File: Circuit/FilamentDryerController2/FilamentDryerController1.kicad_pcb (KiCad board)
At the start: 2 copper layers, 37 parts, among them J1 PWR, J2 Fan, J3 I2C, J4 Heat, J5 I2C, J6 100k, Q1 IRL540N or IRFZ20 or IRF740 o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, SW1 Push, U1 ATmega328-P, U2 LM7805_TO220, U3 SN74LVC2G06, Y1 16MHz

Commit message: Pcb done.
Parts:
- removed C2: 100nF, SparkFun-Capacitor:C_1206_3216Metric
- removed the C4 at (162.5, 46.5)
- removed the J1 at (56.0, 49.0)
- removed the J4 at (69.5, 37.0)
- removed NT1: NetTie, NetTie:NetTie-2_SMD_Pad2.0mm
- removed NT2: NetTie, NetTie:NetTie-2_SMD_Pad0.5mm
- added J5: Screw_Terminal_01x04, SparkFun-Connector:Screw_Terminal_3.5mm-4, F.Cu at (22.5, 26.5)
- added NT4: Mains, Halojen-Footprints:NetTie-2_SMD_Pad0.2x2.5mm, F.Cu at (30.0, 48.0)
- added PS1: HLK-PM01, Converter_ACDC:Converter_ACDC_Hi-Link_HLK-PMxx, F.Cu at (34.0, 33.5)
- added Q2: T835-600B, Package_TO_SOT_SMD:TO-252-2, F.Cu at (36.4, 53.3)
- added R3: 330R, Resistor_SMD:R_1206_3216Metric, F.Cu at (60.2, 57.1)
- added R4: 330R, Resistor_SMD:R_1206_3216Metric, F.Cu at (26.7, 52.6)
- added R5: 360R, Resistor_SMD:R_1206_3216Metric, F.Cu at (46.7, 50.0)
- added TP10: PD3, SparkFun-Connector:TestPoint-1.25mm, F.Cu at (43.6, 79.2)
- added TP7: PC6, SparkFun-Connector:TestPoint-1.25mm, F.Cu at (43.6, 69.1)
- C1, C3: footprint SparkFun-Capacitor:C_1206_3216Metric -> Capacitor_SMD:C_1206_3216Metric
- C4: renamed from C5; footprint SparkFun-Capacitor:C_1206_3216Metric -> Capacitor_SMD:C_1206_3216Metric
- C5: renamed from C6; footprint SparkFun-Capacitor:C_1206_3216Metric -> Capacitor_SMD:C_1206_3216Metric
- J3: renamed from J2; footprint Connector_JST:JST_XH_B4B-XH-A_1x04_P2.50mm_Vertical -> Connector_JST:JST_XH_B2B-XH-A_1x02_P2.50mm_Vertical
- J4: renamed from J6; footprint Connector_JST:JST_XH_B2B-XH-AM_1x02_P2.50mm_Vertical -> Connector_JST:JST_XH_B2B-XH-A_1x02_P2.50mm_Vertical
- NT3: value NetTie -> Mains; footprint NetTie:NetTie-2_SMD_Pad0.5mm -> Halojen-Footprints:NetTie-2_SMD_Pad0.2x2.5mm
- Q1: value IRL540N or IRFZ20 or IRF740 or FDS6690A -> FDS6690A; footprint digikey-footprints:TO-220-3 -> Package_SO:SOIC-8_3.9x4.9mm_P1.27mm
- R1: value 10k -> 100k
- SW1: footprint SparkFun-Switch:Push_SMD_6.2x6.2mm -> Button_Switch_SMD:SW_SPST_PTS645
- TP1: renamed from TP11; value PB2 -> PB0; footprint SparkFun-Connector:1x01 -> SparkFun-Connector:TestPoint-1.25mm
- TP11: renamed from TP8; footprint SparkFun-Connector:1x01 -> SparkFun-Connector:TestPoint-1.25mm
- TP12: renamed from TP9; footprint SparkFun-Connector:1x01 -> SparkFun-Connector:TestPoint-1.25mm
- TP13: renamed from TP10; footprint SparkFun-Connector:1x01 -> SparkFun-Connector:TestPoint-1.25mm
- TP2: renamed from TP1; footprint SparkFun-Connector:1x01 -> SparkFun-Connector:TestPoint-1.25mm
- TP3: renamed from TP2; footprint SparkFun-Connector:1x01 -> SparkFun-Connector:TestPoint-1.25mm
- TP4: renamed from TP3; footprint SparkFun-Connector:1x01 -> SparkFun-Connector:TestPoint-1.25mm
- TP5: renamed from TP4; footprint SparkFun-Connector:1x01 -> SparkFun-Connector:TestPoint-1.25mm
- TP6: renamed from TP5; footprint SparkFun-Connector:1x01 -> SparkFun-Connector:TestPoint-1.25mm
- TP8: renamed from TP6; footprint SparkFun-Connector:1x01 -> SparkFun-Connector:TestPoint-1.25mm
- TP9: renamed from TP7; footprint SparkFun-Connector:1x01 -> SparkFun-Connector:TestPoint-1.25mm
- U2: value LM7805_TO220 -> MOC3043M; footprint Package_TO_SOT_THT:TO-220-3_Vertical -> Package_DIP:SMDIP-6_W9.53mm
- moved C3 127.4 mm to (42.0, 83.1), turned to 180 degrees
- moved NT3 124.2 mm to (40.6, 48.0), turned to 180 degrees
- moved C1 115.0 mm to (59.7, 86.7), turned to 90 degrees
- moved TP11 89.9 mm to (40.6, 79.2)
- moved TP9 87.7 mm to (43.6, 74.2)
- moved TP8 87.3 mm to (43.6, 71.6)
- moved TP12 86.9 mm to (40.6, 99.6)
- moved TP1 84.1 mm to (43.7, 102.1)
- moved TP13 84.1 mm to (43.6, 99.6)
- moved J3 82.8 mm to (22.6, 70.1), turned to 90 degrees
- moved TP5 70.8 mm to (59.6, 76.7)
- moved TP6 70.2 mm to (59.6, 74.2)
- moved TP4 67.8 mm to (59.6, 79.2)
- moved TP3 61.4 mm to (59.6, 97.0)
- moved TP2 60.8 mm to (59.6, 99.6)
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- renumbered J3 to J1, J5 to J2, R3 to R6
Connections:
- C4 pad 2: GNDS -> GND
- C5 pad 1: GNDS -> GND
- J3 pad 1: GND -> +5V
- J3 pad 2: +12V -> Net-(J3-Pin_2)
- J4 pad 1: +5VS -> +5V
- NT3 pad 1: GND -> Net-(NT3-Pad1)
- NT3 pad 2: GNDS -> +AC
- Q1 pad 1: /pHeat -> GND
- Q1 pad 2: Net-(J4-Pin_2) -> GND
- Q1 pad 3: GND12V -> GND
- R1 pad 1: /pHeat -> /pFan_pwm
- R1 pad 2: GNDS -> GND
- R2 pad 2: GNDS -> GND
- SW1 pad 1: GNDS -> GND
- U2 pad 1: +12V -> +5V
- U2 pad 2: GND -> Net-(R3-Pad2)
- U2 pad 3: +5V -> unconnected-(U2-NC-Pad3)
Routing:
- net +5V: track 0.00 -> 182.5 mm, vias 0 -> 4
- net /pHeat: track 0.00 -> 53.5 mm
- net GND: track 0.00 -> 48.1 mm, vias 0 -> 3
- net /pFan_pwm: track 0.00 -> 47.7 mm
- net +AC: track 0.00 -> 36.7 mm
- net /pSCL: track 0.00 -> 34.8 mm
- net /pSDA: track 0.00 -> 32.7 mm, vias 0 -> 1
- net Net-(Q2-G): track 0.00 -> 24.3 mm
- net /pButt: track 0.00 -> 18.3 mm
- net /pTemp: track 0.00 -> 18.2 mm
- net Heater: track 0.00 -> 17.7 mm
- net -AC: track 0.00 -> 17.1 mm
- net Net-(R5-Pad1): track 0.00 -> 13.4 mm, vias 0 -> 2
- net Net-(J3-Pin_2): track 0.00 -> 11.0 mm
- net Net-(U1-PD6): track 0.00 -> 8.16 mm
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- added copper zone on F.Cu, net (none)
- added copper zone on B.Cu, net GND
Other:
- board outline added: 54.1 x 82.3 mm
- board text added: "Filament dryer v0.1 2025 Halojen Productions"
- board text added: "H"
- board text added: "L"
- board text added: "N"

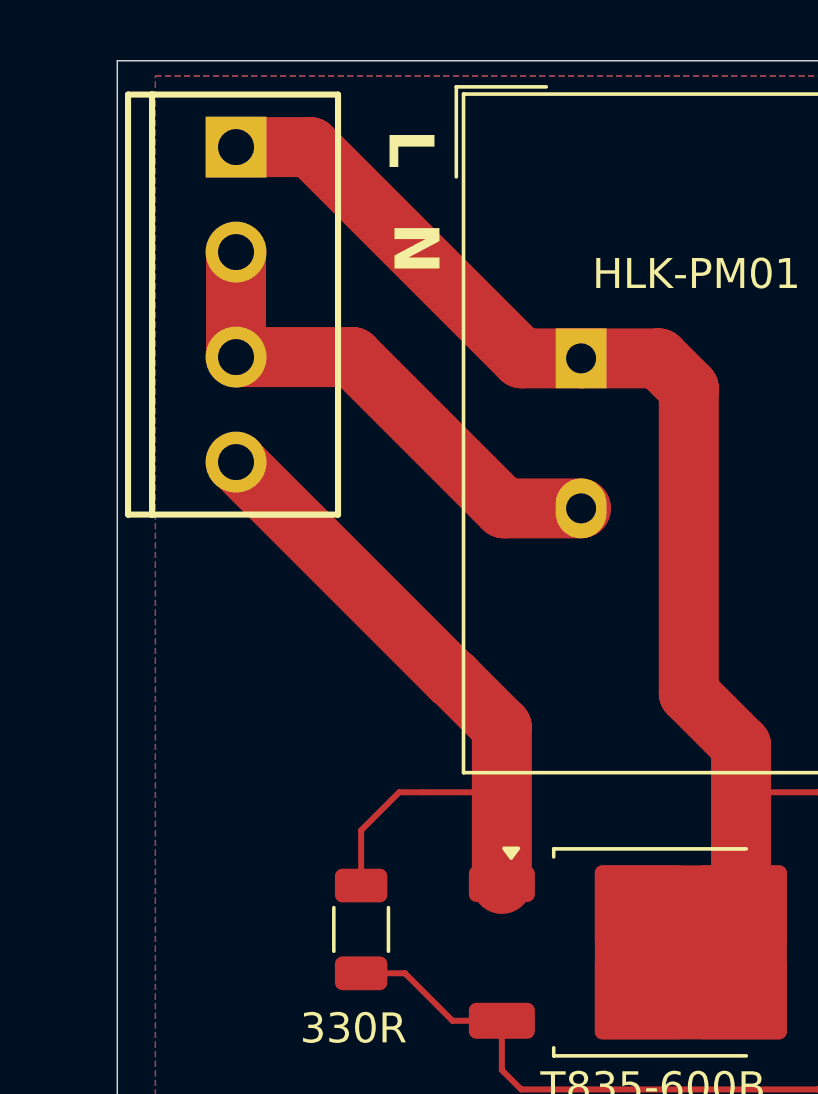
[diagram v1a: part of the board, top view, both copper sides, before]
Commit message: First pcb prototype fabricated.
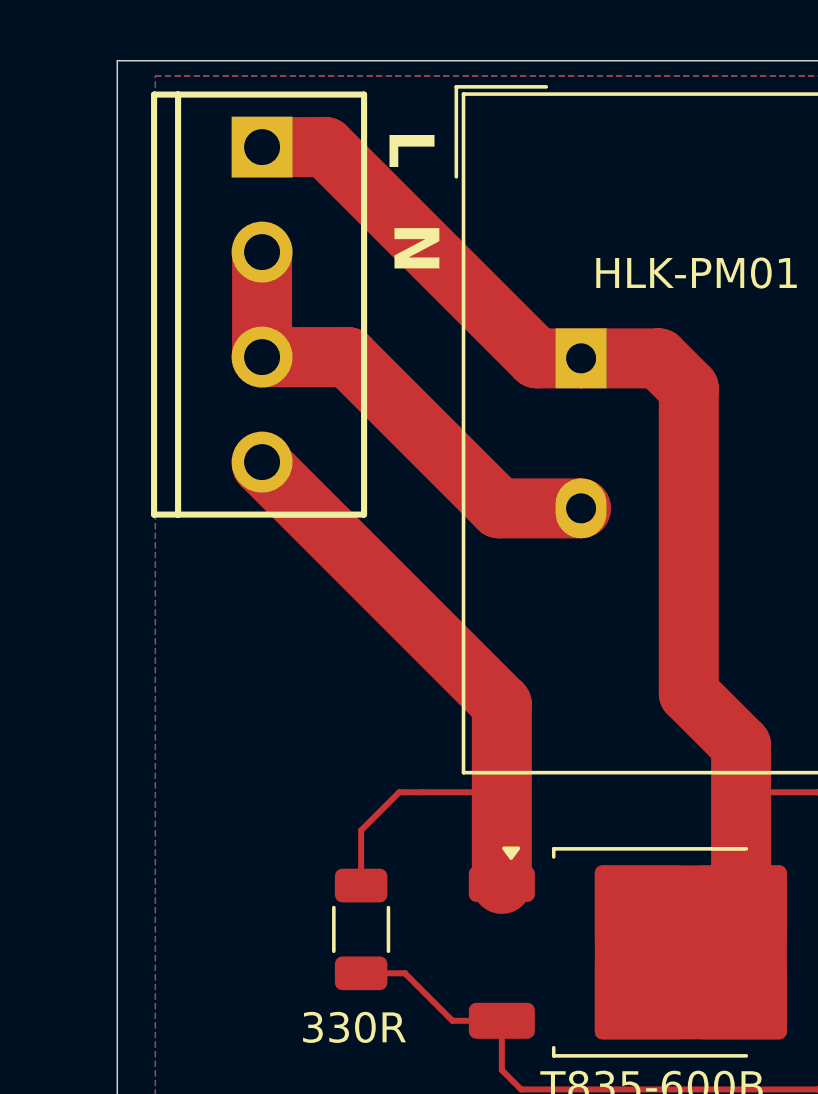
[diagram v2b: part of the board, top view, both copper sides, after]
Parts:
- moved J5 0.87 mm to (23.4, 26.5)
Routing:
- net -AC: track 17.1 -> 16.2 mm
- net +AC: track 36.7 -> 35.8 mm
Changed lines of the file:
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@@
 		(allow_soldermask_bridges_in_footprints no)
 		(pcbplotparams
-			(layerselection 0x00010fc_ffffffff)
+			(layerselection 0x00010f0_ffffffff)
 			(plot_on_all_layers_selection 0x0000000_00000000)
 			(disableapertmacros no)
-			(usegerberextensions no)
+			(usegerberextensions yes)
 			(usegerberattributes yes)
 			(usegerberadvancedattributes yes)
-			(creategerberjobfile yes)
+			(creategerberjobfile no)
 			(dashed_line_dash_ratio 12.000000)
 			(dashed_line_gap_ratio 3.000000)
 			(svgprecision 4)
 			(plotframeref no)
-			(viasonmask no)
+			(viasonmask yes)
 			(mode 1)
 			(useauxorigin no)
@@
 			(psnegative no)
 			(psa4output no)
-			(plotreference yes)
+			(plotreference no)
 			(plotvalue yes)
 			(plotfptext yes)
 			(plotinvisibletext no)
 			(sketchpadsonfab no)
-			(subtractmaskfromsilk no)
+			(subtractmaskfromsilk yes)
 			(outputformat 1)
 			(mirror no)
-			(drillshape 1)
+			(drillshape 0)
 			(scaleselection 1)
-			(outputdirectory "")
+			(outputdirectory "Gerbers/")
 		)
 	)
@@
 		(tags "SMD DIP DIL PDIP SMDIP 2.54mm 9.53mm 375mil")
 		(property "Reference" "U2"
-			(at 0 -4.87 360)
+			(at 0 -4.87 0)
 			(layer "F.SilkS")
 			(hide yes)
@@
 		)
 		(property "Value" "MOC3043M"
-			(at 0.193 -5.08 360)
+			(at 0.193 -5.08 0)
 			(layer "F.SilkS")
 			(effects
@@
 		)
 		(fp_text user "${REFERENCE}"
-			(at 0 0 360)
+			(at 0 0 0)
 			(layer "F.Fab")
 			(effects
@@
 		(tags "resistor")
 		(property "Reference" "R2"
-			(at 0 -1.82 360)
+			(at 0 -1.82 0)
 			(layer "F.SilkS")
 			(hide yes)
@@
 		)
 		(property "Value" "100k"
-			(at 0 1.82 360)
+			(at 0 1.82 0)
 			(layer "F.SilkS")
 			(effects
@@
 		)
 		(fp_text user "${REFERENCE}"
-			(at 0 0 360)
+			(at 0 0 0)
 			(layer "F.Fab")
 			(effects
@@
 		(tags "net tie")
 		(property "Reference" "NT3"
-			(at 0 -1.2 360)
+			(at 0 -1.2 0)
 			(layer "F.SilkS")
 			(hide yes)
@@
 		(tags "resistor")
 		(property "Reference" "R3"
-			(at 0 -1.82 360)
+			(at 0 -1.82 0)
 			(layer "F.SilkS")
 			(hide yes)
@@
 		)
 		(property "Value" "330R"
-			(at 0 1.82 360)
+			(at 0 1.82 0)
 			(layer "F.SilkS")
 			(effects
@@
 		)
 		(fp_text user "${REFERENCE}"
-			(at 0 0 360)
+			(at 0 0 0)
 			(layer "F.Fab")
 			(effects
@@
 	(footprint "SparkFun-Connector:Screw_Terminal_3.5mm-4"
 		(layer "F.Cu")
-		(at 22.5 26.5 -90)
+		(at 23.368 26.5 -90)
 		(tags "SparkFun")
 		(property "Reference" "J5"
@@
 		(tags "DPAK TO-252 DPAK-3 TO-252-3 SOT-428")
 		(property "Reference" "Q2"
-			(at 0 -4.5 360)
+			(at 0 -4.5 0)
 			(layer "F.SilkS")
 			(hide yes)
@@
 		)
 		(property "Value" "T835-600B"
-			(at 0 4.5 360)
+			(at 0 4.5 0)
 			(layer "F.SilkS")
 			(effects
@@
 		)
 		(fp_text user "${REFERENCE}"
-			(at 0 0 360)
+			(at 0 0 0)
 			(layer "F.Fab")
 			(effects
@@
 		(tags "resistor")
 		(property "Reference" "R5"
-			(at 0 -1.82 360)
+			(at 0 -1.82 0)
 			(layer "F.SilkS")
 			(hide yes)
@@
 		)
 		(property "Value" "360R"
-			(at 0 1.82 360)
+			(at 0 1.82 0)
 			(layer "F.SilkS")
 			(effects
@@
 		)
 		(fp_text user "${REFERENCE}"
-			(at 0 0 360)
+			(at 0 0 0)
 			(layer "F.Fab")
 			(effects
@@
 		(tags "SOIC SO")
 		(property "Reference" "Q1"
-			(at 0 -3.4 360)
+			(at 0 -3.4 0)
 			(layer "F.SilkS")
 			(hide yes)
@@
 		)
 		(property "Value" "FDS6690A"
-			(at 0 3.4 360)
+			(at 0 3.4 0)
 			(layer "F.SilkS")
 			(effects
@@
 		)
 		(property "Footprint" "Package_SO:SOIC-8_3.9x4.9mm_P1.27mm"
-			(at 0 0 360)
+			(at 0 0 0)
 			(layer "F.Fab")
 			(hide yes)
@@
 		)
 		(property "Datasheet" ""
-			(at 0 0 360)
+			(at 0 0 0)
 			(layer "F.Fab")
 			(hide yes)
@@
 		)
 		(property "Description" "11A, 30V, N-Channel Logic Level MOSFET, SO-8"
-			(at 0 0 360)
+			(at 0 0 0)
 			(layer "F.Fab")
 			(hide yes)
@@
 		)
 		(fp_text user "${REFERENCE}"
-			(at 0 0 360)
+			(at 0 0 0)
 			(layer "F.Fab")
 			(effects
@@
 	)
 	(segment
-		(start 29.718 44.196)
-		(end 31.36 45.838)
+		(start 23.368 37)
+		(end 23.368 37.084)
 		(width 2)
 		(layer "F.Cu")
@@
 	)
 	(segment
-		(start 22.5 37)
-		(end 29.696 44.196)
+		(start 23.368 37.084)
+		(end 31.36 45.076)
 		(width 2)
 		(layer "F.Cu")
@@
 	)
 	(segment
-		(start 31.36 45.838)
+		(start 31.36 45.076)
 		(end 31.36 51.0625)
 		(width 2)
@@
 	)
 	(segment
-		(start 29.696 44.196)
-		(end 29.718 44.196)
-		(width 2)
-		(layer "F.Cu")
-		(net 18)
-	)
-	(segment
 		(start 43.3036 89.408)
 		(end 42.1386 88.243)
@@
 	)
 	(segment
-		(start 22.5 33.5)
-		(end 26.388 33.5)
+		(start 31.27175 38.5425)
+		(end 34.0025 38.5425)
 		(width 2)
 		(layer "F.Cu")
@@
 	)
 	(segment
-		(start 26.388 33.5)
-		(end 31.4305 38.5425)
+		(start 26.22925 33.5)
+		(end 31.27175 38.5425)
 		(width 2)
 		(layer "F.Cu")
@@
 	)
 	(segment
-		(start 22.5 30)
-		(end 22.5 33.5)
+		(start 23.368 30)
+		(end 23.368 33.5)
 		(width 2)
 		(layer "F.Cu")
@@
 	)
 	(segment
-		(start 31.4305 38.5425)
-		(end 34.0025 38.5425)
+		(start 23.368 33.5)
+		(end 26.22925 33.5)
 		(width 2)
 		(layer "F.Cu")
@@
 	)
 	(segment
-		(start 32.0185 33.5425)
-		(end 24.976 26.5)
+		(start 34.0025 33.5425)
+		(end 32.5265 33.5425)
 		(width 2)
 		(layer "F.Cu")
@@
 	)
 	(segment
-		(start 24.976 26.5)
-		(end 22.5 26.5)
+		(start 25.484 26.5)
+		(end 23.368 26.5)
 		(width 2)
 		(layer "F.Cu")
@@
 	)
 	(segment
-		(start 34.0025 33.5425)
-		(end 32.0185 33.5425)
+		(start 32.5265 33.5425)
+		(end 25.484 26.5)
 		(width 2)
 		(layer "F.Cu")
